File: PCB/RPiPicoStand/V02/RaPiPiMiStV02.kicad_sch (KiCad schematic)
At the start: 24 parts, among them J1 Conn_01x04_Pin, J2 Conn_01x04_Pin, J3 Conn_02x20_Counter_Clockwise, J4 Conn_01x04_Pin, J5 Conn_01x02_Pin, SW1 SW_DIP_x03, SW2 SW_DIP_x03, SW3 SW_DIP_x03

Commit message: add V2 kicad project
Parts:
- removed 5VBUCK1: ~, Library:BUCK Converter 5-30V 5V 3A smd, symbol Driver_Motor:BUCK_CONVERTER_5-30V_to_5V_3A
- removed A1, A2, A3: Pololu_Breakout_A4988, Module:Pololu_Breakout-16_15.2x20.3mm, symbol Driver_Motor:Pololu_Breakout_A4988
- removed J3: Conn_02x20_Counter_Clockwise, Connector:DIP-40_709_ELL socket W18Pins W21, symbol Connector_Generic:Conn_02x20_Counter_Clockwise
- removed R1, R2, R3, R4, R5, R6: R_Small, Resistor_THT:R_Axial_DIN0207_L6.3mm_D2.5mm_P10.16mm_Horizontal, symbol Device:R_Small
- removed SW1, SW2, SW3: SW_DIP_x03, Button_Switch_THT:SW_DIP_SPSTx03_Slide_9.78x9.8mm_W7.62mm_P2.54mm, symbol Switch:SW_DIP_x03
- added 5VBUCK2: ~, RaPiPiMiSt:BUCK Converter 5-30V 5V 3A smd, symbol RaPiPiMiSt:BUCK_CONVERTER_5-30V_to_5V_3A
- added J6: Conn_01x04_Pin, Connector_PinSocket_2.54mm:PinSocket_1x04_P2.54mm_Vertical, symbol Connector:Conn_01x04_Pin
- added U1: Pico, MCU_RaspberryPi_and_Boards:RPi_Pico_SMD_TH, symbol MCU_RaspberryPi_and_Boards:Pico
- added U2, U3, U4: TMC2209_SILENTSTEPSTICK, RaPiPiMiSt:MODULE_TMC2209_SILENTSTEPSTICK, symbol RaPiPiMiSt:TMC2209_SILENTSTEPSTICK
- C1, C3, C5: footprint Capacitor_THT:CP_Radial_D7.5mm_P2.50mm -> Capacitor_SMD:CP_Elec_6.3x7.7
- C2, C4, C6: footprint Capacitor_THT:C_Disc_D6.0mm_W2.5mm_P5.00mm -> Capacitor_SMD:C_0603_1608Metric
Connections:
- net GND: now also 5VBUCK2.1 (OUT-), 5VBUCK2.3 (IN-), J6.1 (Pin_1), U1.13 (GND), U1.18 (GND), U1.23 (GND), U1.28 (GND), U1.3 (GND), U1.38 (GND), U1.8 (GND), U2.1 (GND), U2.11 (PDN), U2.13 (SPRD), U2.7 (GND), U3.1 (GND), U3.11 (PDN), U3.13 (SPRD), U3.7 (GND), U4.1 (GND), U4.11 (PDN), U4.13 (SPRD), U4.7 (GND)
- net at C1.1, C2.2, C3.1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: now also 5VBUCK2.2 (IN+), U2.8 (VM), U3.8 (VM), U4.8 (VM)
- net at J2.1 (Pin_1): now also U2.3 (M1B)
- net at J2.2 (Pin_2): now also U2.4 (M1A)
- net at J2.3 (Pin_3): now also U2.5 (M2A)
- net at J2.4 (Pin_4): now also U2.6 (M2B)
- net at J1.1 (Pin_1): now also U3.3 (M1B)
- net at J1.2 (Pin_2): now also U3.4 (M1A)
- net at J1.3 (Pin_3): now also U3.5 (M2A)
- net at J1.4 (Pin_4): now also U3.6 (M2B)
- net at J4.4 (Pin_4): now also U4.6 (M2B)
- net at J4.3 (Pin_3): now also U4.5 (M2A)
- net at J4.2 (Pin_2): now also U4.4 (M1A)
- net at J4.1 (Pin_1): now also U4.3 (M1B)
- new net: J6.2 (Pin_2), U1.17 (GPIO13)
- new net: J6.3 (Pin_3), U1.20 (GPIO15)
- new net: J6.4 (Pin_4), U1.19 (GPIO14)
- new net: U1.6 (GPIO4), U3.10 (STEP)
- new net: U1.1 (GPIO0), U1.2 (GPIO1), U3.12 (UART)
- new net: 5VBUCK2.0 (OUT+), U1.39 (VSYS), U2.14 (MS2), U2.15 (MS1), U2.2 (VIO), U3.14 (MS2), U3.15 (MS1), U3.2 (VIO), U4.14 (MS2), U4.15 (MS1), U4.2 (VIO)
- new net: U1.4 (GPIO2), U3.16 (~{EN})
- new net: U1.5 (GPIO3), U3.18 (DIAG)
- new net: U1.7 (GPIO5), U3.9 (DIR)
- new net: U1.26 (GPIO20), U4.10 (STEP)
- new net: U1.21 (GPIO16), U1.22 (GPIO17), U4.12 (UART)
- new net: U1.25 (GPIO19), U4.16 (~{EN})
- new net: U1.24 (GPIO18), U4.18 (DIAG)
- new net: U1.27 (GPIO21), U4.9 (DIR)
- new net: U1.10 (GPIO7), U2.18 (DIAG)
- new net: U1.11 (GPIO8), U1.12 (GPIO9), U2.12 (UART)
- new net: U1.14 (GPIO10), U2.16 (~{EN})
- new net: U1.15 (GPIO11), U2.10 (STEP)
- new net: U1.16 (GPIO12), U2.9 (DIR)
- no-connect marks 26 -> 17
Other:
- moved on the sheet: C1, C2, C3, C4, C5, C6, J1, J2, J4

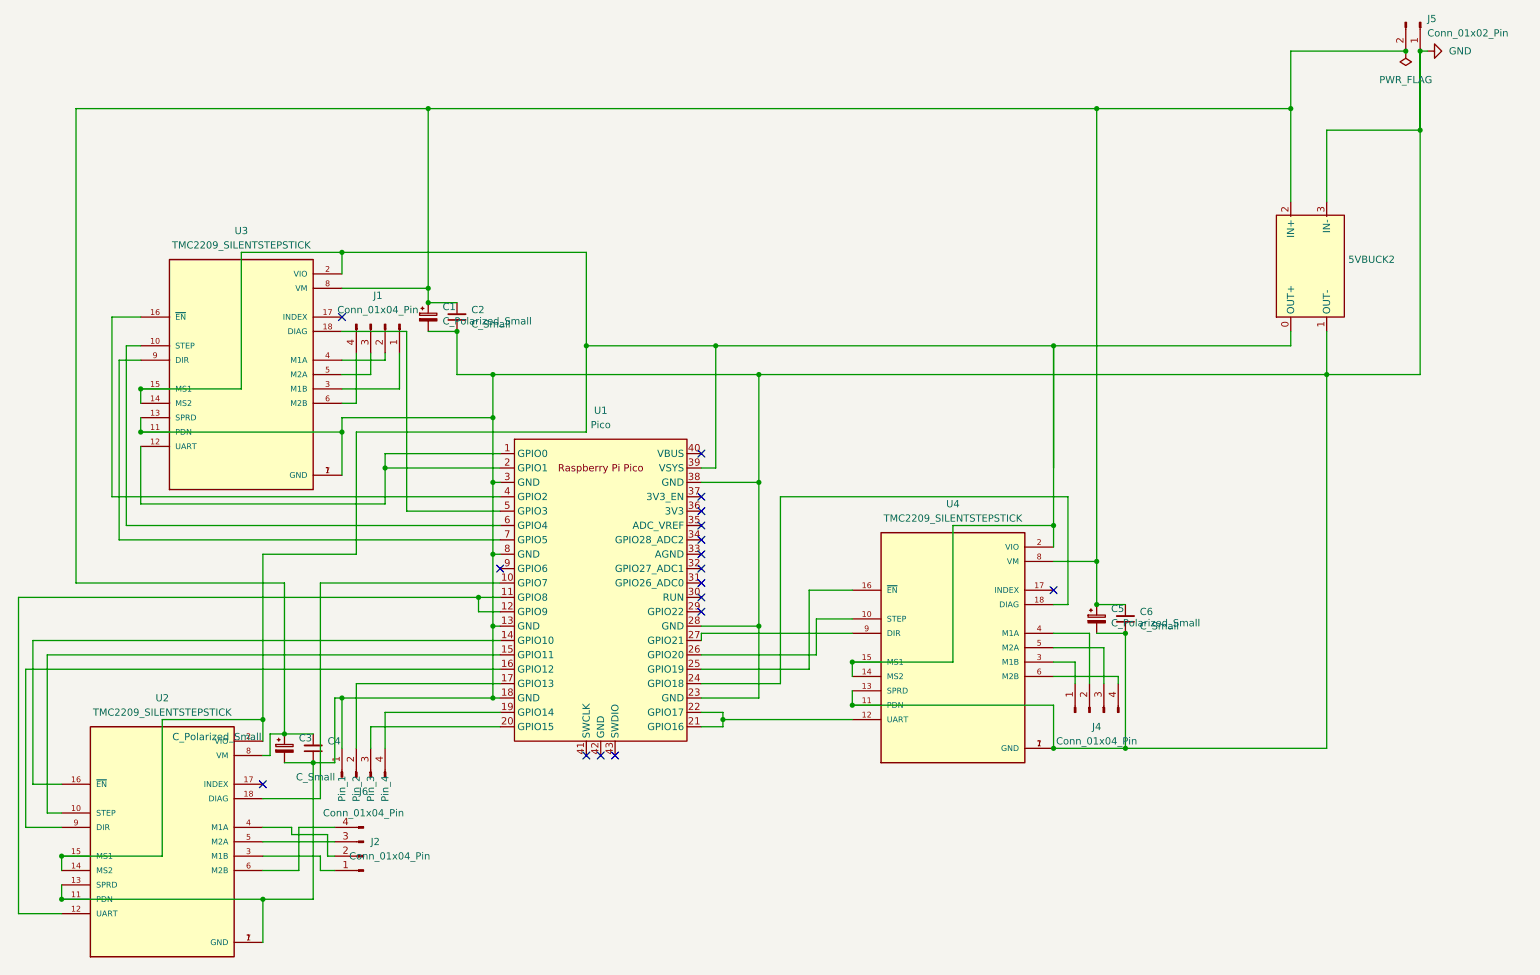
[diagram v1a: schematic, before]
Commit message: Remove legacy frontend and backend code for RPi Pico Mic Stand
Deleted unused `index.html` and `main.py` to clean up the repository. This removes obsolete web interface scripts, hardware control logic, and display effects to prepare for a streamlined implementation.
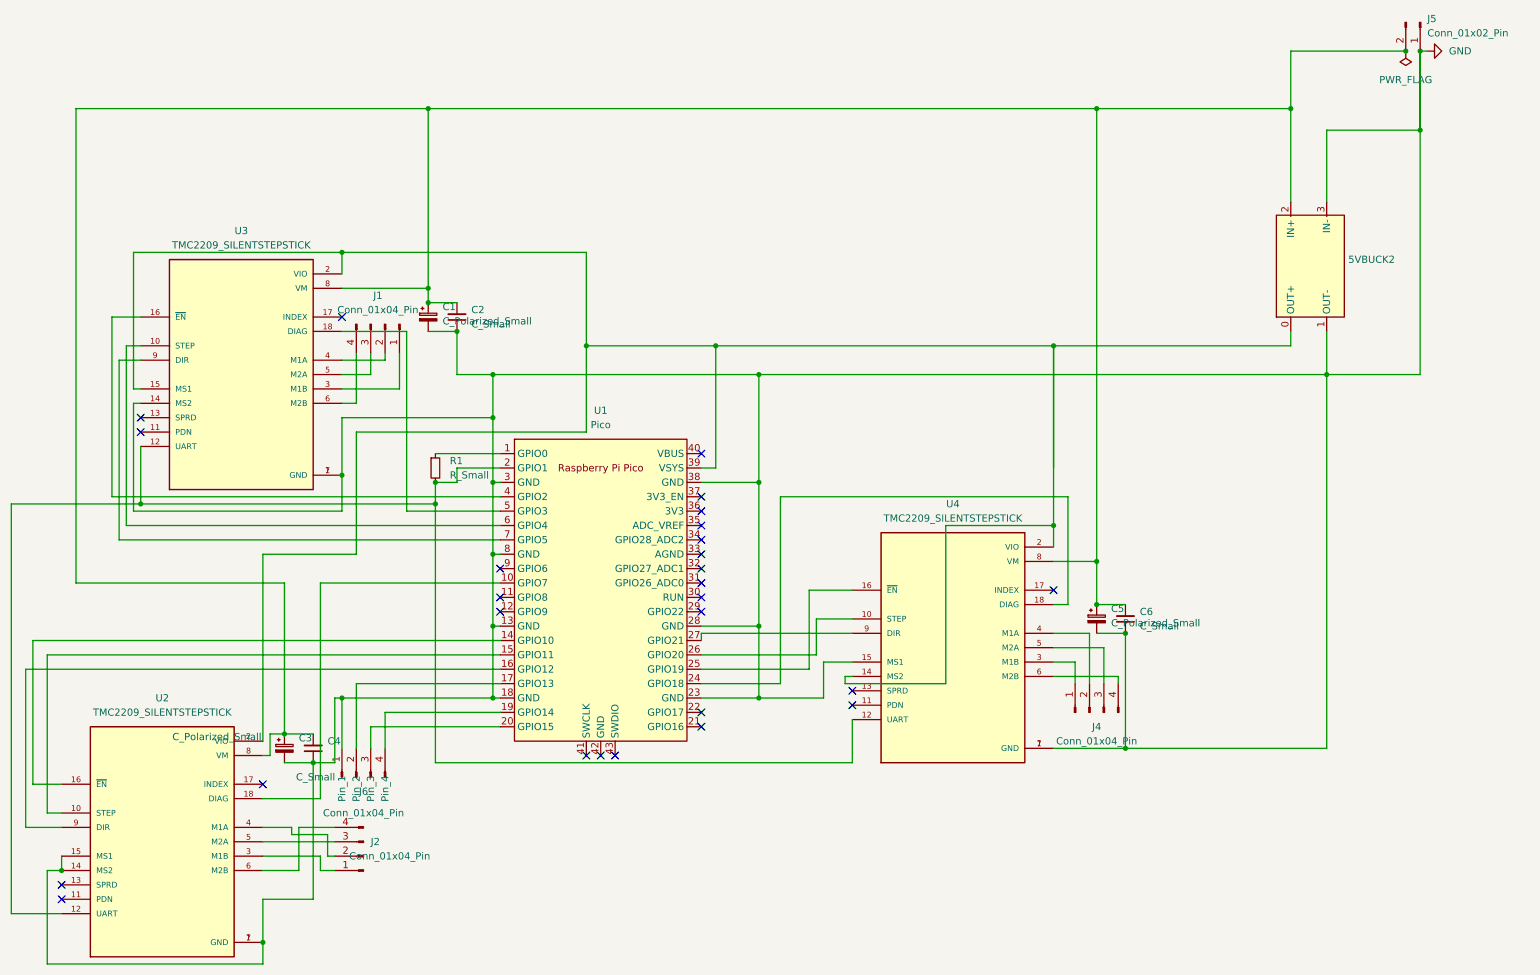
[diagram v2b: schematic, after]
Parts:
- added R1: R_Small, Resistor_SMD:R_0603_1608Metric_Pad0.98x0.95mm_HandSolder, symbol Device:R_Small
- 5VBUCK2: footprint RaPiPiMiSt:BUCK Converter 5-30V 5V 3A smd -> Library:BUCK Converter 5-30V 5V 3A smd
- U2, U3, U4: footprint RaPiPiMiSt:MODULE_TMC2209_SILENTSTEPSTICK -> Motors:MODULE_TMC2209_SILENTSTEPSTICK
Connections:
- net GND: now also U2.14 (MS2), U2.15 (MS1), U3.14 (MS2), U4.15 (MS1); no longer U2.11 (PDN), U2.13 (SPRD), U3.11 (PDN), U3.13 (SPRD), U4.11 (PDN), U4.13 (SPRD)
- net at U1.2 (GPIO1), U3.12 (UART): now also U2.12 (UART), U4.12 (UART), R1.2; no longer U1.1 (GPIO0)
- net at 5VBUCK2.0 (OUT+), U1.39 (VSYS), U2.2 (VIO)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: no longer U2.14 (MS2), U2.15 (MS1), U3.14 (MS2), U4.15 (MS1)
- new net: R1.1, U1.1 (GPIO0)
- now unconnected: U1.11 (GPIO8), U1.12 (GPIO9), U1.21 (GPIO16), U1.22 (GPIO17)
- no-connect marks 17 -> 27

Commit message: fix uart connections on the PCB
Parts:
- 5VBUCK2: footprint Library:BUCK Converter 5-30V 5V 3A smd -> RaPiPiMiSt:BUCK Converter 5-30V 5V 3A smd
- U2, U3, U4: footprint Motors:MODULE_TMC2209_SILENTSTEPSTICK -> RaPiPiMiSt:MODULE_TMC2209_SILENTSTEPSTICK
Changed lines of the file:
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@@
 			)
 		)
-		(property "Footprint" "Motors:MODULE_TMC2209_SILENTSTEPSTICK"
+		(property "Footprint" "RaPiPiMiSt:MODULE_TMC2209_SILENTSTEPSTICK"
 			(at 67.31 86.36 0)
 			(effects
@@
 			)
 		)
-		(property "Footprint" "Motors:MODULE_TMC2209_SILENTSTEPSTICK"
+		(property "Footprint" "RaPiPiMiSt:MODULE_TMC2209_SILENTSTEPSTICK"
 			(at 193.04 134.62 0)
 			(effects
@@
 			)
 		)
-		(property "Footprint" "Library:BUCK Converter 5-30V 5V 3A smd"
+		(property "Footprint" "RaPiPiMiSt:BUCK Converter 5-30V 5V 3A smd"
 			(at 250.19 76.2 0)
 			(effects
@@
 			)
 		)
-		(property "Footprint" "Motors:MODULE_TMC2209_SILENTSTEPSTICK"
+		(property "Footprint" "RaPiPiMiSt:MODULE_TMC2209_SILENTSTEPSTICK"
 			(at 53.34 168.91 0)
 			(effects
